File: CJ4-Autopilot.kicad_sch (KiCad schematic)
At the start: 38 parts, among them J1 Conn_01x05, J2 Conn_01x05, J3 Conn_01x05, J4 Conn_01x05, SW1 SW_Push_LED, SW10 SW_Push_LED, SW11 SW_Push_LED, SW12 SW_Push_LED, SW13 SW_Push_LED, SW14 SW_Push_LED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

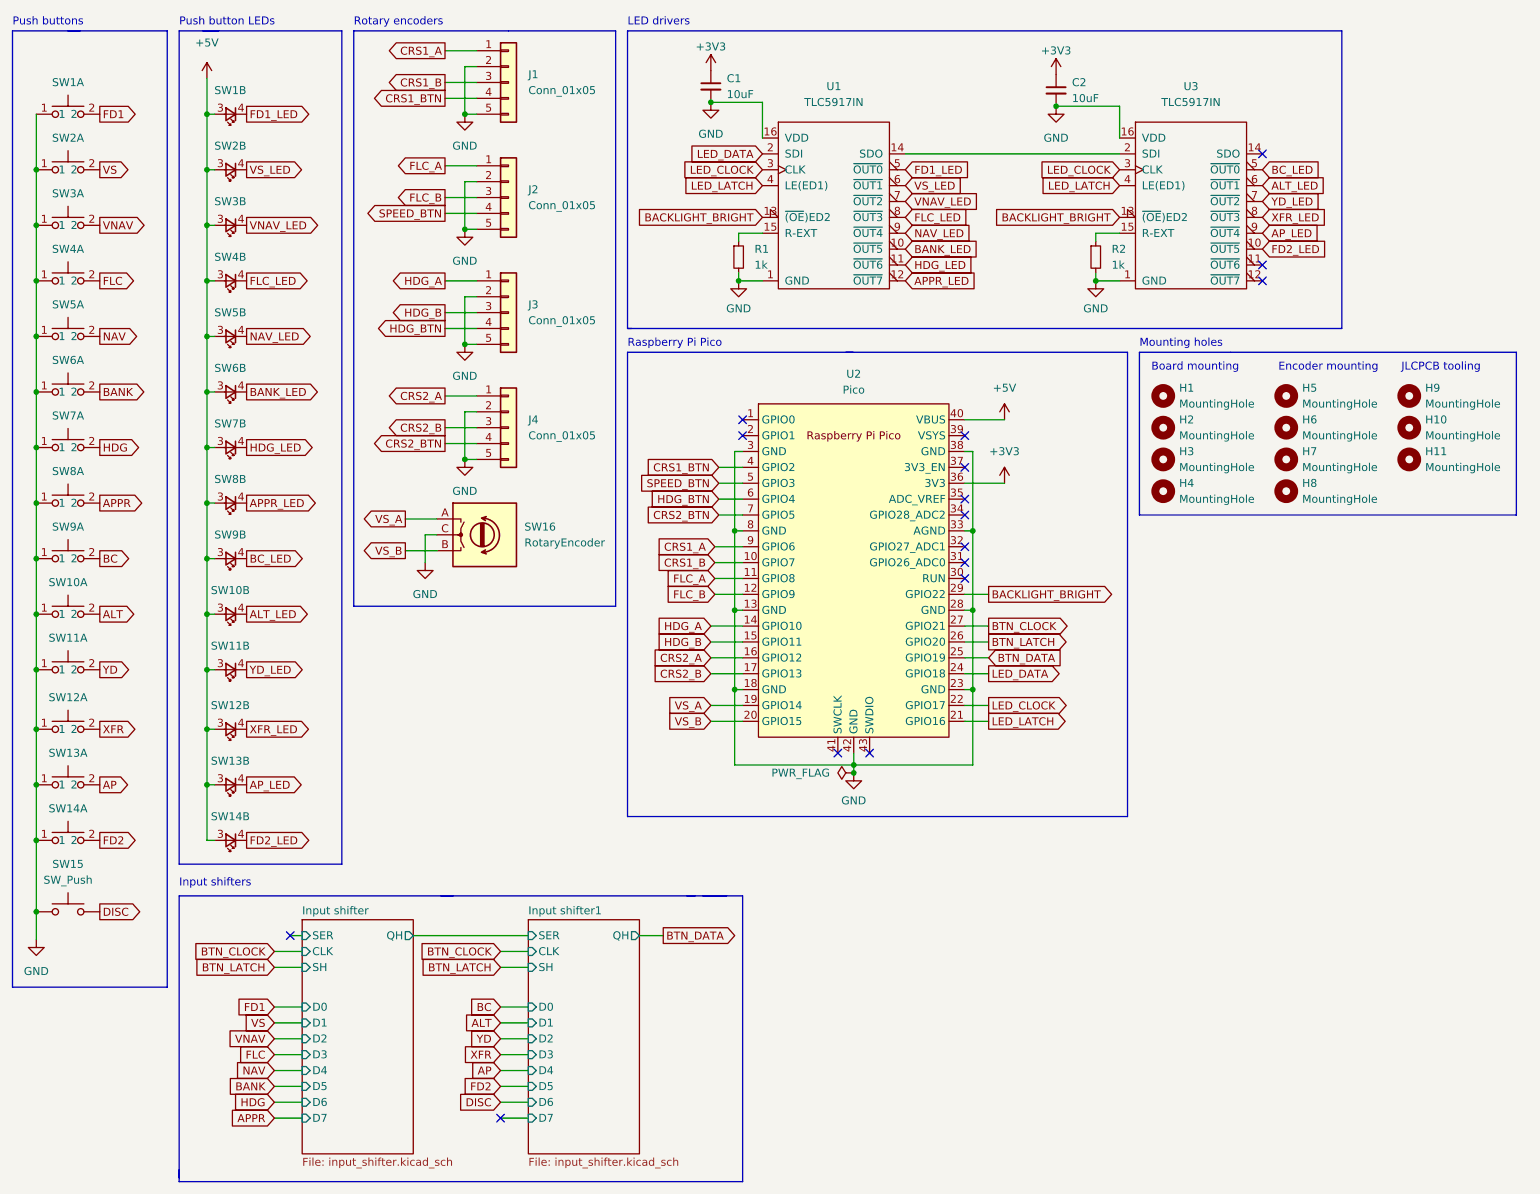
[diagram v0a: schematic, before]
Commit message: Initial board layout, still a lot of work to do
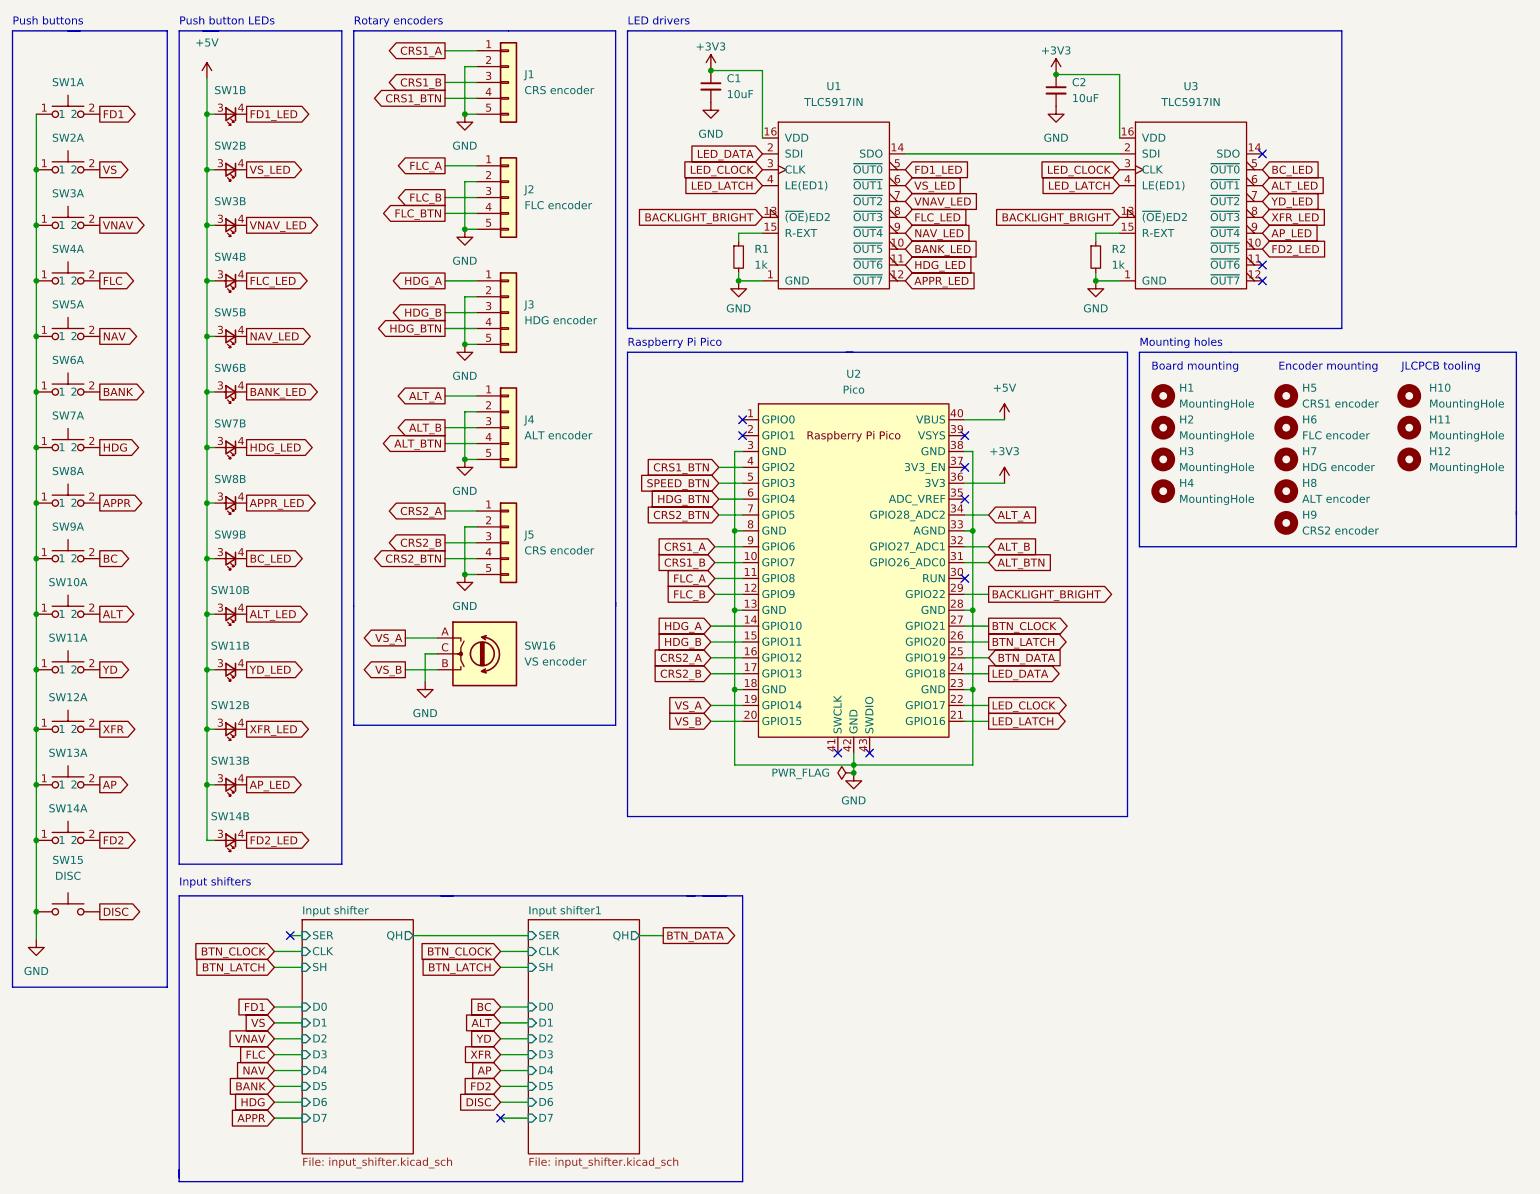
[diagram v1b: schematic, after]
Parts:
- added H9: CRS2 encoder, CJ4-Autopilot:MountingHole_7.5mm, symbol Mechanical:MountingHole
- added J5: CRS encoder, Connector_JST:JST_XA_B05B-XASK-1_1x05_P2.50mm_Vertical, symbol Connector_Generic:Conn_01x05
- H10: renamed from H9; footprint MountingHole:MountingHole_3.2mm_M3 -> CJ4-Autopilot:JLCPCB_Tooling_Hole
- H11: renamed from H10; footprint MountingHole:MountingHole_3.2mm_M3 -> CJ4-Autopilot:JLCPCB_Tooling_Hole
- H12: renamed from H11; footprint MountingHole:MountingHole_3.2mm_M3 -> CJ4-Autopilot:JLCPCB_Tooling_Hole
- H5: value MountingHole -> CRS1 encoder
- H6: value MountingHole -> FLC encoder
- H7: value MountingHole -> HDG encoder
- H8: value MountingHole -> ALT encoder
- J1: value Conn_01x05 -> CRS encoder; footprint CJ4-Autopilot:SW_PUSH_6mm -> Connector_JST:JST_XA_B05B-XASK-1_1x05_P2.50mm_Vertical
- J2: value Conn_01x05 -> FLC encoder; footprint CJ4-Autopilot:SW_PUSH_6mm -> Connector_JST:JST_XA_B05B-XASK-1_1x05_P2.50mm_Vertical
- J3: value Conn_01x05 -> HDG encoder; footprint CJ4-Autopilot:SW_PUSH_6mm -> Connector_JST:JST_XA_B05B-XASK-1_1x05_P2.50mm_Vertical
- J4: value Conn_01x05 -> ALT encoder; footprint CJ4-Autopilot:SW_PUSH_6mm -> Connector_JST:JST_XA_B05B-XASK-1_1x05_P2.50mm_Vertical
- R1, R2: footprint CJ4-Autopilot:SW_PUSH_6mm -> Resistor_SMD:R_0603_1608Metric
- SW1: value SW_Push_LED -> FD1
- SW10: value SW_Push_LED -> ALT
- SW11: value SW_Push_LED -> YD
- SW12: value SW_Push_LED -> XFR
- SW13: value SW_Push_LED -> AP
- SW14: value SW_Push_LED -> FD2
- SW15: value SW_Push -> DISC
- SW16: value RotaryEncoder -> VS encoder
- SW2: value SW_Push_LED -> VS
- SW3: value SW_Push_LED -> VNAV
- SW4: value SW_Push_LED -> FLC
- SW5: value SW_Push_LED -> NAV
- SW6: value SW_Push_LED -> BANK
- SW7: value SW_Push_LED -> HDG
- SW8: value SW_Push_LED -> APPR
- SW9: value SW_Push_LED -> BC
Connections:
- net +3V3: now also U1.16 (VDD), U3.16 (VDD)
- net CRS2_A: now also J5.1 (Pin_1); no longer J4.1 (Pin_1)
- net CRS2_B: now also J5.3 (Pin_3); no longer J4.3 (Pin_3)
- net CRS2_BTN: now also J5.4 (Pin_4); no longer J4.4 (Pin_4)
- net GND: now also J5.2 (Pin_2), J5.5 (Pin_5); no longer U1.16 (VDD), U3.16 (VDD)
- net SPEED_BTN: no longer J2.4 (Pin_4)
- net ALT_BTN: now reaches U2.31 (GPIO26_ADC0)
- net ALT_BTN: now also J4.4 (Pin_4)
- net ALT_B: now reaches U2.32 (GPIO27_ADC1)
- net ALT_B: now also J4.3 (Pin_3)
- net ALT_A: now reaches U2.34 (GPIO28_ADC2)
- net ALT_A: now also J4.1 (Pin_1)
- new net FLC_BTN: J2.4 (Pin_4)
- no-connect marks 16 -> 13
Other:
- moved on the sheet: SW16

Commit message: Add RP2040 directly to the board
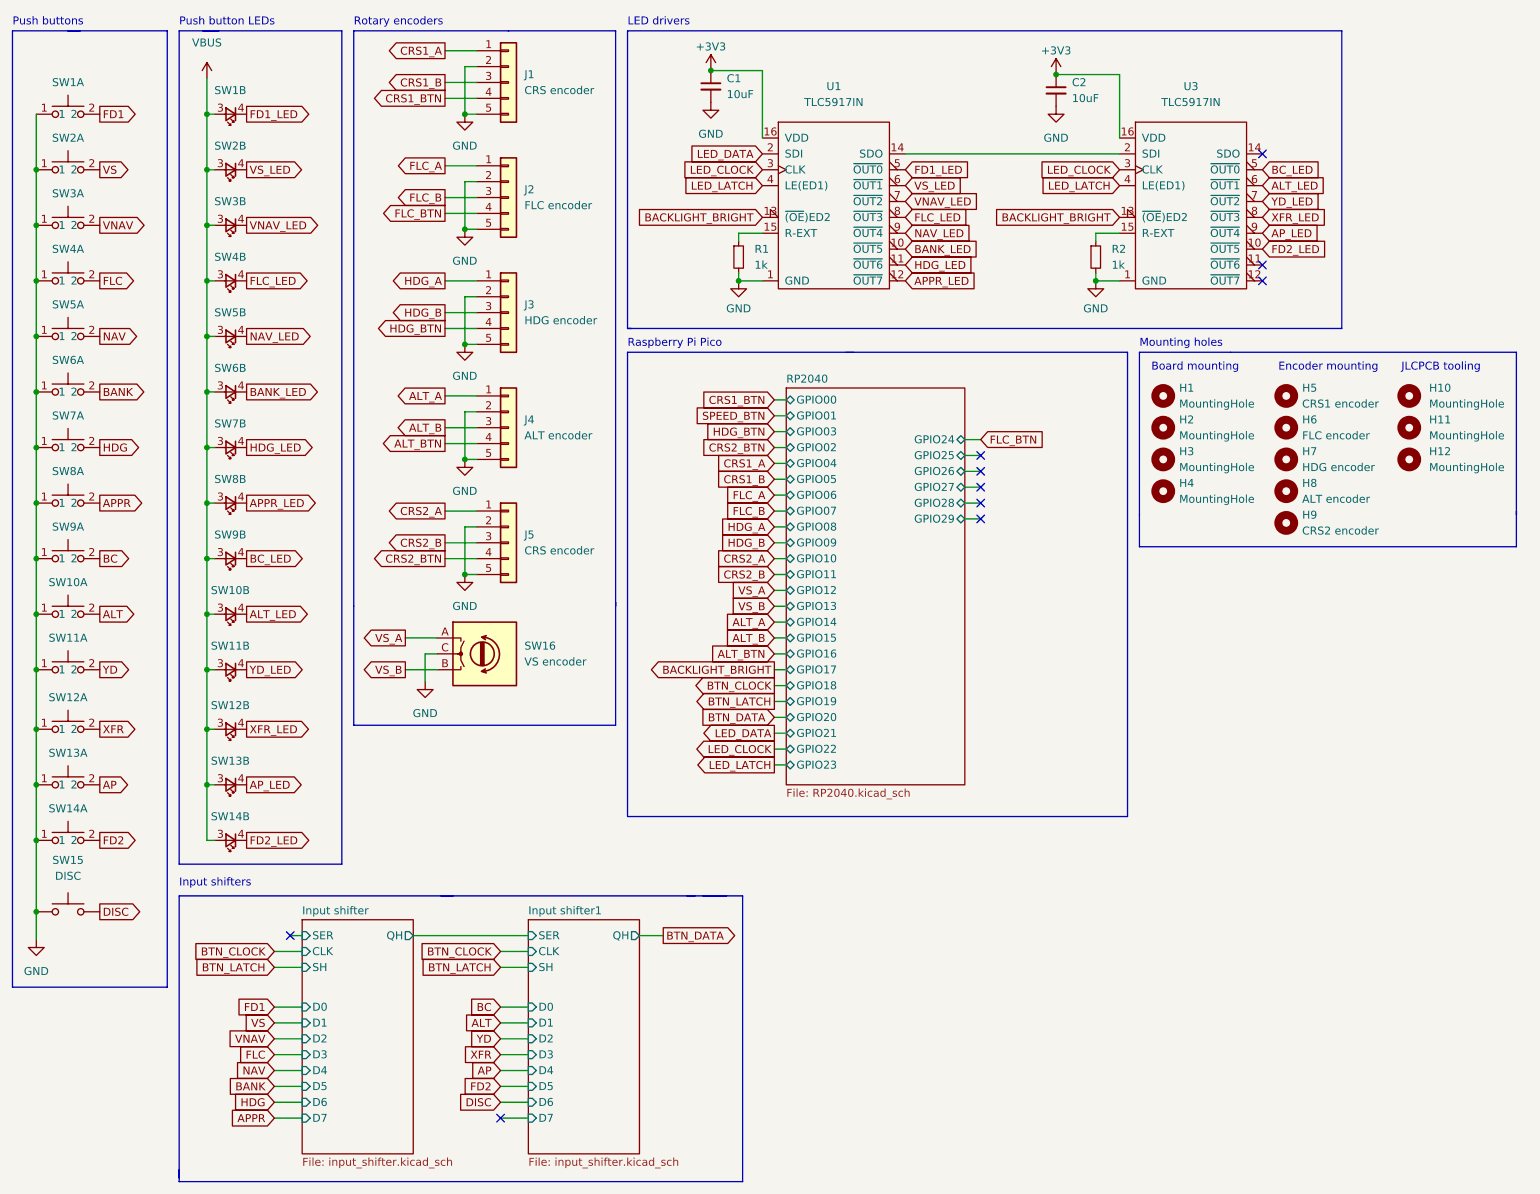
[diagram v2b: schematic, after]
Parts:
- removed U2: Pico, MCU_RaspberryPi_and_Boards:RPi_Pico_SMD_TH, symbol MCU_RaspberryPi_and_Boards:Pico
- C1, C2: JLC (none) -> 0603; LCSC (none) -> C19702
- J1, J2, J3, J4, J5: footprint Connector_JST:JST_XA_B05B-XASK-1_1x05_P2.50mm_Vertical -> Connector_JST:JST_XH_B5B-XH-A_1x05_P2.50mm_Vertical
- R1, R2: footprint Resistor_SMD:R_0603_1608Metric -> CJ4-Autopilot:Perfect_0402; JLC 0603 -> 0402; LCSC C21190 -> C11702
- U1, U3: footprint Package_DIP:DIP-16_W7.62mm -> Package_SO:SOIC-16_3.9x9.9mm_P1.27mm
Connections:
- net +5V renamed VBUS
- no-connect marks 13 -> 10
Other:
- added sheet RP2040 (RP2040.kicad_sch)

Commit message: Update encoder footprint, USB trace width
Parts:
- H5, H6, H7, H8, H9: footprint CJ4-Autopilot:MountingHole_7.5mm -> CJ4-Autopilot:EN11-HSM1BF20 panel mount
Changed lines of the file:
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@@
       (effects (font (size 1.27 1.27)) (justify right))
     )
-    (property "Footprint" "CJ4-Autopilot:MountingHole_7.5mm" (id 2) (at 217.17 79.375 0)
+    (property "Footprint" "CJ4-Autopilot:EN11-HSM1BF20 panel mount" (id 2) (at 217.17 79.375 0)
       (effects (font (size 1.27 1.27)) hide)
     )
@@
       (effects (font (size 1.27 1.27)) (justify right))
     )
-    (property "Footprint" "CJ4-Autopilot:MountingHole_7.5mm" (id 2) (at 217.17 89.535 0)
+    (property "Footprint" "CJ4-Autopilot:EN11-HSM1BF20 panel mount" (id 2) (at 217.17 89.535 0)
       (effects (font (size 1.27 1.27)) hide)
     )
@@
       (effects (font (size 1.27 1.27)) (justify right))
     )
-    (property "Footprint" "CJ4-Autopilot:MountingHole_7.5mm" (id 2) (at 217.17 84.455 0)
+    (property "Footprint" "CJ4-Autopilot:EN11-HSM1BF20 panel mount" (id 2) (at 217.17 84.455 0)
       (effects (font (size 1.27 1.27)) hide)
     )
@@
       (effects (font (size 1.27 1.27)) (justify right))
     )
-    (property "Footprint" "CJ4-Autopilot:MountingHole_7.5mm" (id 2) (at 217.17 74.295 0)
+    (property "Footprint" "CJ4-Autopilot:EN11-HSM1BF20 panel mount" (id 2) (at 217.17 74.295 0)
       (effects (font (size 1.27 1.27)) hide)
     )
@@
       (effects (font (size 1.27 1.27)) (justify right))
     )
-    (property "Footprint" "CJ4-Autopilot:MountingHole_7.5mm" (id 2) (at 217.17 94.615 0)
+    (property "Footprint" "CJ4-Autopilot:EN11-HSM1BF20 panel mount" (id 2) (at 217.17 94.615 0)
       (effects (font (size 1.27 1.27)) hide)
     )
@@
     )
     (path "/6754165e-2250-4aa6-ba75-67e8dfe043b1"
-      (reference "H5") (unit 1) (value "CRS1 encoder") (footprint "CJ4-Autopilot:MountingHole_7.5mm")
+      (reference "H5") (unit 1) (value "CRS1 encoder") (footprint "CJ4-Autopilot:EN11-HSM1BF20 panel mount")
     )
     (path "/28a8cb81-6091-43c6-926b-932e4ea8a929"
-      (reference "H6") (unit 1) (value "FLC encoder") (footprint "CJ4-Autopilot:MountingHole_7.5mm")
+      (reference "H6") (unit 1) (value "FLC encoder") (footprint "CJ4-Autopilot:EN11-HSM1BF20 panel mount")
     )
     (path "/62f0366f-694e-4e09-907d-36fee04ab834"
-      (reference "H7") (unit 1) (value "HDG encoder") (footprint "CJ4-Autopilot:MountingHole_7.5mm")
+      (reference "H7") (unit 1) (value "HDG encoder") (footprint "CJ4-Autopilot:EN11-HSM1BF20 panel mount")
     )
     (path "/4686e682-4f45-482f-93af-91cf386c60d9"
-      (reference "H8") (unit 1) (value "ALT encoder") (footprint "CJ4-Autopilot:MountingHole_7.5mm")
+      (reference "H8") (unit 1) (value "ALT encoder") (footprint "CJ4-Autopilot:EN11-HSM1BF20 panel mount")
     )
     (path "/e205c85d-545e-4caf-a814-f7d0e94d19fe"
-      (reference "H9") (unit 1) (value "CRS2 encoder") (footprint "CJ4-Autopilot:MountingHole_7.5mm")
+      (reference "H9") (unit 1) (value "CRS2 encoder") (footprint "CJ4-Autopilot:EN11-HSM1BF20 panel mount")
     )
     (path "/29d1cfd7-23f9-4de3-8e8d-9a936a1debd7"
